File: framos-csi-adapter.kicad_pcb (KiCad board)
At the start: 4 copper layers, 26.5 x 26.5 mm, 71 parts, among them J1 DF40C-60DS-0.4V(51), J2 MSAK24025P30, U1 NTS0102GT, U2 AP62301Z6-7, U3 AP62301Z6-7

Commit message: Bump revision to 1.1.0
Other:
- board text added: "Framos CSI adapter Rev. 1.1.0 06/2022"
- board text removed: "Framos CSI adapter Rev. 1.0.0 02/2022"
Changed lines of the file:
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@@
   )
   (paper "A4")
+  (title_block
+    (title "FRAMOS CSI adapter")
+    (date "2022-06-30")
+    (rev "1.1.0")
+  )
   (layers
     (0 "F.Cu" signal)
@@
   (gr_arc (start 126.5 124.25) (mid 125.84099 125.84099) (end 124.25 126.5) (layer "Edge.Cuts") (width 0.05))
   (gr_arc (start 124.25 100) (mid 125.84099 100.65901) (end 126.5 102.25) (layer "Edge.Cuts") (width 0.05))
-  (gr_text "Framos CSI adapter\nRev. 1.0.0 02/2022" (at 125.15 104.6 90) (layer "F.Cu")
+  (gr_text "Framos CSI adapter\nRev. 1.1.0 06/2022" (at 125.15 104.6 90) (layer "F.Cu")
     (effects (font (size 0.65 0.65) (thickness 0.15)) (justify right))
   )
@@
     (effects (font (size 0.7 0.7) (thickness 0.15)))
   )
-  (gr_text "Framos CSI adapter\nRev. 1.0.0 02/2022" (at 125.15 104.6 90) (layer "F.Mask")
+  (gr_text "Framos CSI adapter\nRev. 1.1.0 06/2022" (at 125.15 104.6 90) (layer "F.Mask")
     (effects (font (size 0.65 0.65) (thickness 0.15)) (justify right))
   )

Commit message: Migrate to KiCad 6. Add LICENSE and README. Correct OSHW logo footprint
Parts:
- removed the REF** at (123.6, 119.0)
- added N1: oshw_logo, framos-csi-adapter-footprints:OSHW-Logo2_7.3x6mm_Copper, F.Cu at (123.6, 119.0)
- U1: footprint antmicro-footprints:PSON50P100X195X50-8N -> framos-csi-adapter-footprints:PSON50P100X195X50-8N
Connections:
- J1 pad 16: Net-(J1-Pad16) -> unconnected-(J1-Pad16)
- J1 pad 17: Net-(J1-Pad17) -> unconnected-(J1-Pad17)
- J1 pad 20: Net-(J1-Pad20) -> unconnected-(J1-Pad20)
- J1 pad 22: Net-(J1-Pad22) -> unconnected-(J1-Pad22)
- J1 pad 24: Net-(J1-Pad24) -> unconnected-(J1-Pad24)
- J1 pad 26: Net-(J1-Pad26) -> unconnected-(J1-Pad26)
- J1 pad 28: Net-(J1-Pad28) -> unconnected-(J1-Pad28)
- J1 pad 40: Net-(J1-Pad40) -> unconnected-(J1-Pad40)
- J1 pad 42: Net-(J1-Pad42) -> unconnected-(J1-Pad42)
- J1 pad 45: Net-(J1-Pad45) -> unconnected-(J1-Pad45)
- J1 pad 47: Net-(J1-Pad47) -> unconnected-(J1-Pad47)
- TP18 pad 1: Net-(TP18-Pad1) -> unconnected-(TP18-Pad1)
- TP6 pad 1: Net-(TP6-Pad1) -> unconnected-(TP6-Pad1)
- U2 pad 5: Net-(TP6-Pad1) -> unconnected-(TP6-Pad1)
- U3 pad 5: Net-(TP18-Pad1) -> unconnected-(TP18-Pad1)
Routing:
- net unconnected-(TP18-Pad1): track 0.00 -> 2.06 mm
- net Net-(TP18-Pad1): track 2.06 -> 0.00 mm
- net unconnected-(TP6-Pad1): track 0.00 -> 1.10 mm
- net Net-(TP6-Pad1): track 1.10 -> 0.00 mm

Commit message: Cleanup
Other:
- board text added: "FRAMOS CSI adapter Rev. 1.1.0 06/2022"
- board text removed: "Framos CSI adapter Rev. 1.1.0 06/2022"
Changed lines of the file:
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@@
   (gr_arc (start 126.5 124.25) (mid 125.84099 125.84099) (end 124.25 126.5) (layer "Edge.Cuts") (width 0.05))
   (gr_arc (start 124.25 100) (mid 125.84099 100.65901) (end 126.5 102.25) (layer "Edge.Cuts") (width 0.05))
-  (gr_text "Framos CSI adapter\nRev. 1.1.0 06/2022" (at 125.15 104.6 90) (layer "F.Cu")
+  (gr_text "FRAMOS CSI adapter\nRev. 1.1.0 06/2022" (at 125.15 104.6 90) (layer "F.Cu")
     (effects (font (size 0.65 0.65) (thickness 0.15)) (justify right))
   )
@@
     (effects (font (size 0.7 0.7) (thickness 0.15)))
   )
-  (gr_text "Framos CSI adapter\nRev. 1.1.0 06/2022" (at 125.15 104.6 90) (layer "F.Mask")
+  (gr_text "FRAMOS CSI adapter\nRev. 1.1.0 06/2022" (at 125.15 104.6 90) (layer "F.Mask")
     (effects (font (size 0.65 0.65) (thickness 0.15)) (justify right))
   )

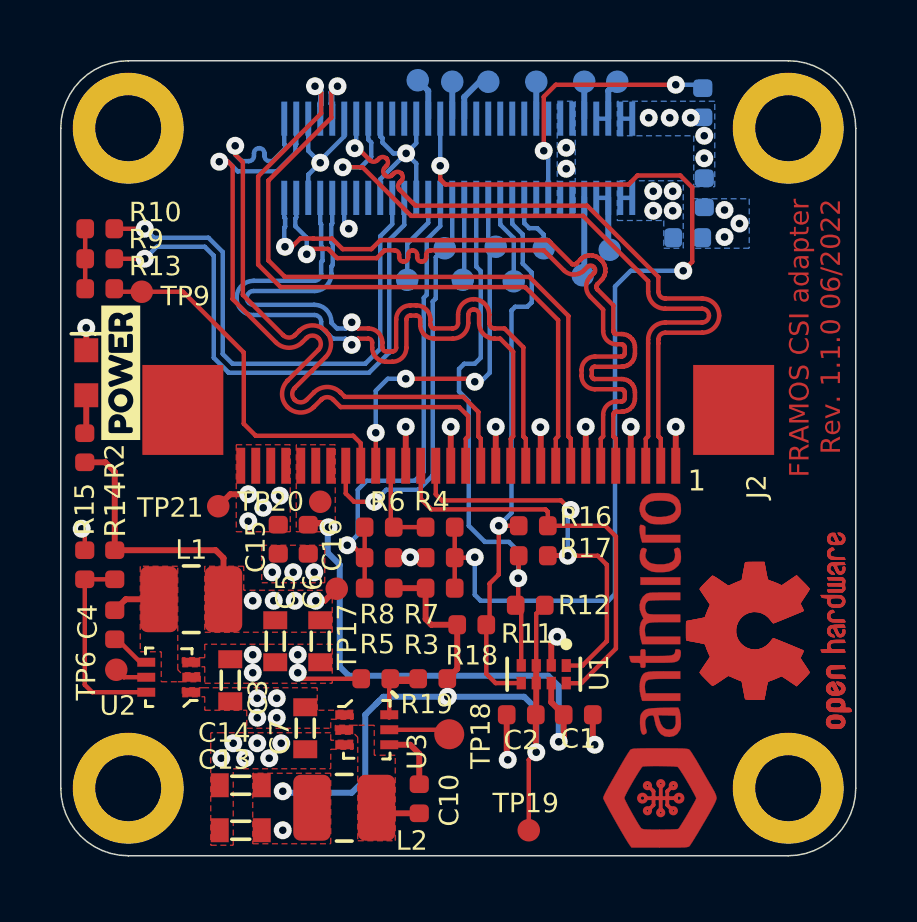
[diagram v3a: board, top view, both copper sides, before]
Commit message: Introduce component standardization
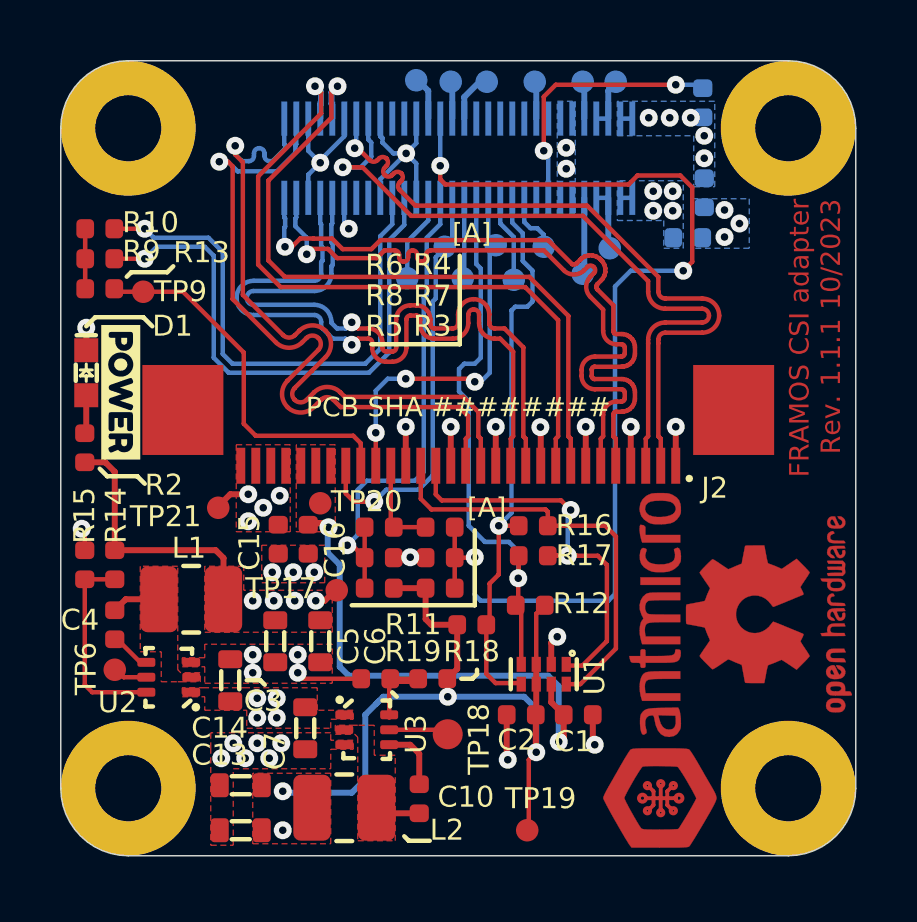
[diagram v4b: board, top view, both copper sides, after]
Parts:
- removed REF**: OSHW-Logo2_7.3x6mm_Copper_Mask, framos-csi-adapter-footprints:OSHW-Logo2_7.3x6mm_Copper_Mask
- removed REF**: MSAK24025P30_PLUG, framos-csi-adapter-footprints:MSAK24025P30_PLUG
- C1, C10, C12, C15, C16, C2, C4, C8: footprint framos-csi-adapter-footprints:0402-cap -> antmicro-footprints:C_0402_1005Metric
- C13, C14, C3, C5, C6, C7: footprint framos-csi-adapter-footprints:0603-cap -> antmicro-footprints:C_0603_1608Metric
- D1: value KP-1608CGCK -> LED_G_0603_KP-1608CGCK; footprint framos-csi-adapter-footprints:LED_0603 -> antmicro-footprints:LED_0603_1608Metric_G
- J1: value DF40C-60DS-0.4V(51) -> Conn_Hirose_DF40C-60DS-0.4V51; footprint framos-csi-adapter-footprints:DF40C-60DS-0.4V51 -> antmicro-footprints:Conn_Hirose_DF40C-60DS-0.4V51
- J2: value MSAK24025P30 -> Conn_STM_MSAK24025P30; footprint framos-csi-adapter-footprints:MSAK24025P30 -> antmicro-footprints:Conn_STM_MSAK24025P30
- L1, L2: footprint framos-csi-adapter-footprints:L_1008_2520Metric -> antmicro-footprints:L_1008_2520Metric
- MP1, MP2, MP3, MP4: footprint framos-csi-adapter-footprints:mounting-hole-2.2mm -> antmicro-footprints:mounting-hole-2.2mm
- N1: footprint framos-csi-adapter-footprints:OSHW-Logo2_7.3x6mm_Copper -> antmicro-footprints:OSHW-Logo2_7.3x6mm_Copper_Mask
- N2: footprint framos-csi-adapter-footprints:antmicro-logo_scaled_12mm -> antmicro-footprints:antmicro-logo_scaled_12mm
- R1, R10, R11, R12, R13, R14, R15, R16, R17, R18, R19, R2, R3, R4, R5, R6, R7, R8, R9: footprint framos-csi-adapter-footprints:0402-res -> antmicro-footprints:R_0402_1005Metric
- TP1, TP10, TP11, TP12, TP13, TP14, TP15, TP16, TP17, TP19, TP2, TP20, TP21, TP3, TP4, TP5, TP6, TP7, TP8, TP9: value TP_SMD_0_75MM -> TP_0.75mm_SMD; footprint framos-csi-adapter-footprints:Testpoint_smd_0_75mm -> antmicro-footprints:TP_SMD_0.75mm
- TP18: value TP_SMD1MM -> TP_1mm_SMD; footprint framos-csi-adapter-footprints:Testpoint_smd_1mm -> antmicro-footprints:Testpoint_smd_1mm
- U1: value NTS0102GT -> NTS0102_XSON; footprint framos-csi-adapter-footprints:PSON50P100X195X50-8N -> antmicro-footprints:XSON-8_1x1.95mm_P0.5mm
- U2, U3: footprint framos-csi-adapter-footprints:SOT-563 -> antmicro-footprints:SOT-563
- moved J2 2.47 mm to (113.2, 111.6)
- moved kibuzzard-621A77E1 0.65 mm to (102.0, 111.0), turned to -90 degrees
- moved N1 0.55 mm to (123.6, 118.5)
- moved TP9 0.07 mm to (102.8, 107.7)
- turned C10 to -90 degrees
- turned C4 to 90 degrees
- turned D1 to 90 degrees
- turned R3 to 0 degrees
- turned U2 to 180 degrees
- turned U3 to 0 degrees
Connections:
- L1 pad 1: Net-(C4-Pad1) -> Net-(C4-Pad2)
- L2 pad 1: Net-(C10-Pad1) -> Net-(C10-Pad2)
- R3 pad 1: /PW_EN_1 -> 1V8_CAM
- R3 pad 2: 1V8_CAM -> /PW_EN_1
- TP18 pad 1: unconnected-(TP18-Pad1) -> Net-(TP18-Pad1)
- TP6 pad 1: unconnected-(TP6-Pad1) -> Net-(TP6-Pad1)
- U2 pad 2: Net-(C4-Pad1) -> Net-(C4-Pad2)
- U2 pad 4: Net-(C4-Pad2) -> Net-(C4-Pad1)
- U2 pad 5: unconnected-(TP6-Pad1) -> Net-(TP6-Pad1)
- U3 pad 2: Net-(C10-Pad1) -> Net-(C10-Pad2)
- U3 pad 4: Net-(C10-Pad2) -> Net-(C10-Pad1)
- U3 pad 5: unconnected-(TP18-Pad1) -> Net-(TP18-Pad1)
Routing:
- net unconnected-(TP18-Pad1): track 2.06 -> 0.00 mm
- net Net-(TP18-Pad1): track 0.00 -> 2.06 mm
- net unconnected-(TP6-Pad1): track 1.10 -> 0.00 mm
- net Net-(TP6-Pad1): track 0.00 -> 1.10 mm
- net Net-(C10-Pad2): track 2.14 -> 1.50 mm
- net Net-(C10-Pad1): track 1.50 -> 2.14 mm
- added copper zone on F.Cu, net Net-(C10-Pad2)
- added copper zone on F.Cu, net Net-(C4-Pad2)
- removed copper zone on F.Cu, net Net-(C10-Pad1)
- removed copper zone on F.Cu, net Net-(C4-Pad1)
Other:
- board text added: "FRAMOS CSI adapter Rev. 1.1.1 10/2023"
- board text added: "PCB SHA ########"
- board text added: "[A]"
- board text removed: "FRAMOS CSI adapter Rev. 1.1.0 06/2022"
